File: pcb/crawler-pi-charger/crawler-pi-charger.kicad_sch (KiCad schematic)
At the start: 8 parts, among them J1 DOCK_15V, J2 SYSTEM_8V, J3 BUCK_IN_15V, J4 BUCK_OUT_8V, J5 NTC, J6 BAT_7V2, Q1 FDS6975, U1 LTC4011CFE

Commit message: Add charger MOSFETs and Wurth inductor symbols
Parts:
- added Q2: FDC658AP, Package_TO_SOT_SMD:SuperSOT-6, symbol crawler-pi-charger:FDC658AP
- added Q3: SI3434DV, Package_SO:TSOP-6_1.65x3.05mm_P0.95mm, symbol crawler-pi-charger:SI3434DV
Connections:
- net at Q1.7 (D): no longer Q1.8 (D)
- net at Q1.5 (D): no longer Q1.6 (D)
- new net SW: Q2.1 (D), Q2.2 (D), Q2.5 (D), Q2.6 (D), Q3.1 (D), Q3.2 (D), Q3.5 (D), Q3.6 (D)

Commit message: Add UPS140 Schottky diode and charger components
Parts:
- added D1: UPS140, Diode_SMD:D_Powermite_LargeCathode, symbol crawler-pi-charger:UPS140
- added L1: 10.0 uH, crawler:L_Wurth_WE-LHMI-7050, symbol crawler-pi-charger:WURTH74437349100
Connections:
- net GND: now also D1.2 (A)
- net SW: now also D1.1 (K), L1.1
- net BGATE: now reaches U1.15 (BGATE)
- net BGATE: now also Q3.3 (G)
- net TGATE: now reaches U1.17 (TGATE)
- net TGATE: now also Q2.3 (G)

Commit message: Input and PowerPath & Battery Charger (Switching Buck Converter)
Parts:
- removed J3: BUCK_IN_15V, TerminalBlock:TerminalBlock_bornier-2_P5.08mm, symbol Connector_Generic:Conn_01x02
- removed J4: BUCK_OUT_8V, TerminalBlock:TerminalBlock_bornier-2_P5.08mm, symbol Connector_Generic:Conn_01x02
- added C1, C2: 10uF, Capacitor_SMD:C_1210_3225Metric, symbol crawler-pi-charger:TMK325BJ106MM
- added D1: MMSZ5248BS-7, Diode_SMD:D_SOD-323, symbol crawler-pi-charger:MMSZ5248BS
- added R1: 47k, Resistor_SMD:R_0402_1005Metric, symbol crawler-pi-charger:CRCW040247K0JNED
- added R6: 0.05, Resistor_SMD:R_1206_3216Metric, symbol crawler-pi-charger:ERJ-L08KJ50MV
- J1: value DOCK_15V -> DOCK_12V3
- renumbered D1 to D6
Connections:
- net DOCK_15V_RAW is gone; now on net DOCK_12V3: J1.1 (Pin_1)
- net GND: now also J2.1 (Pin_1), J2.2 (Pin_2), J6.2 (Pin_2), Q1.1 (S), Q1.3 (S), Q2.4 (S), Q3.4 (S), U1.16 (PGND), U1.18 (V_{CC}), U1.21 (GND), U1.5 (GND), C1.1, C1.2, C2.2, D1.1 (K)
- net DOCK_12V3: now reaches U1.1 (DCIN)
- net DOCK_12V3: now also Q1.7 (D), Q1.8 (D), R1.1
- net SENSE: now reaches U1.11 (SENSE)
- net SENSE: now also L1.2, R6.1
- net BAT_7V2: now reaches U1.12 (BAT)
- net BAT_7V2: now also J6.1 (Pin_1), Q1.5 (D), Q1.6 (D), C2.1, R6.2
- net INFET: now reaches U1.20 (INFET)
- net INFET: now also Q1.2 (G)
- net Q1B_GATE: now reaches Q1.4 (G)
- net Q1B_GATE: now also D1.2 (A), R1.2
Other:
- moved on the sheet: D6, J2, J6, L1, Q1A, Q1B, Q2, Q3, U1

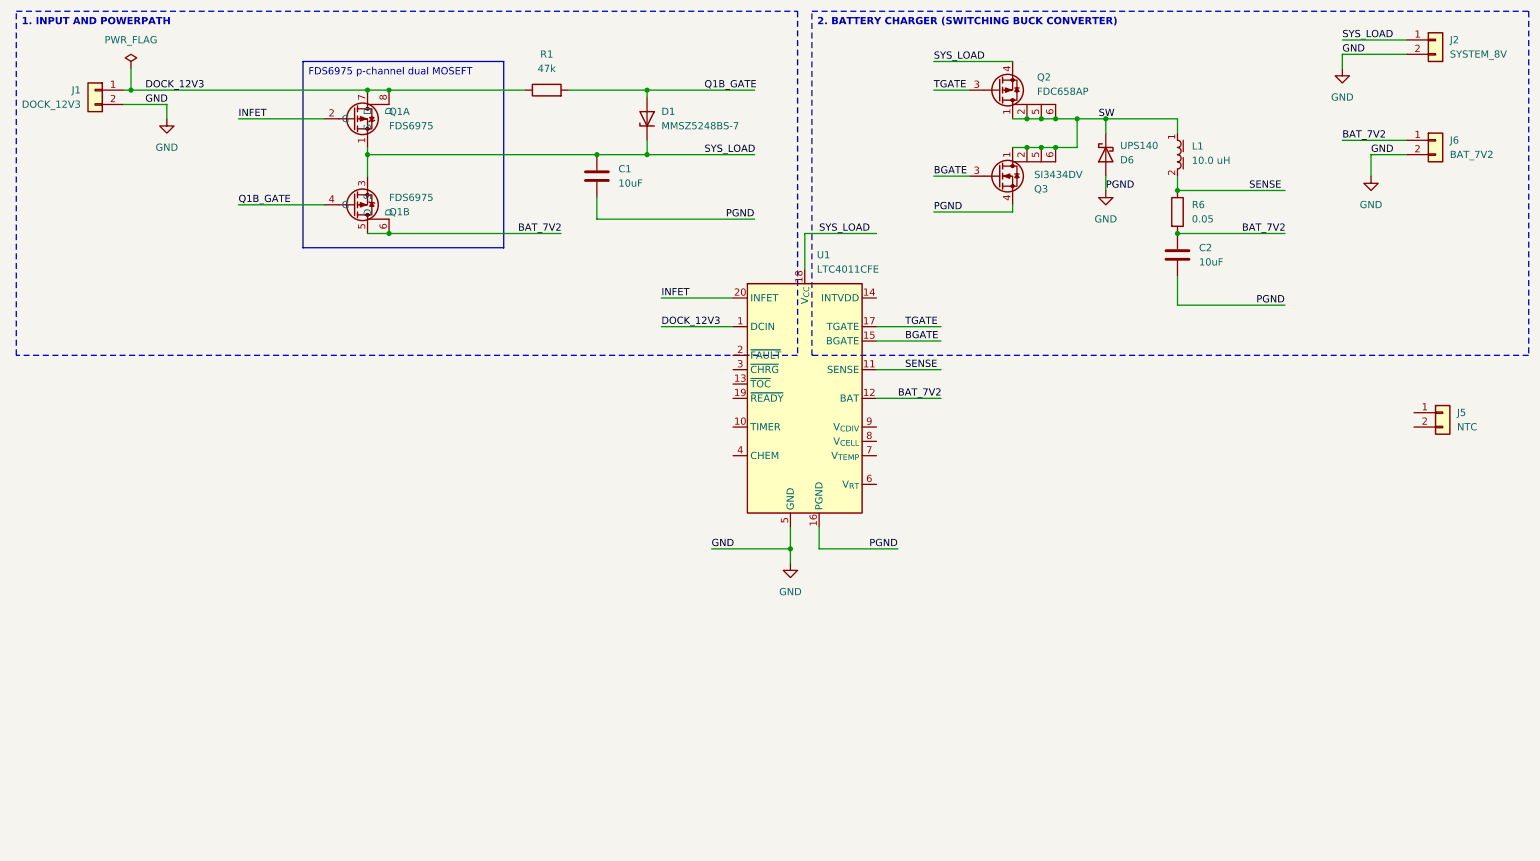
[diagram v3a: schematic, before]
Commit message: Battery Monitoring
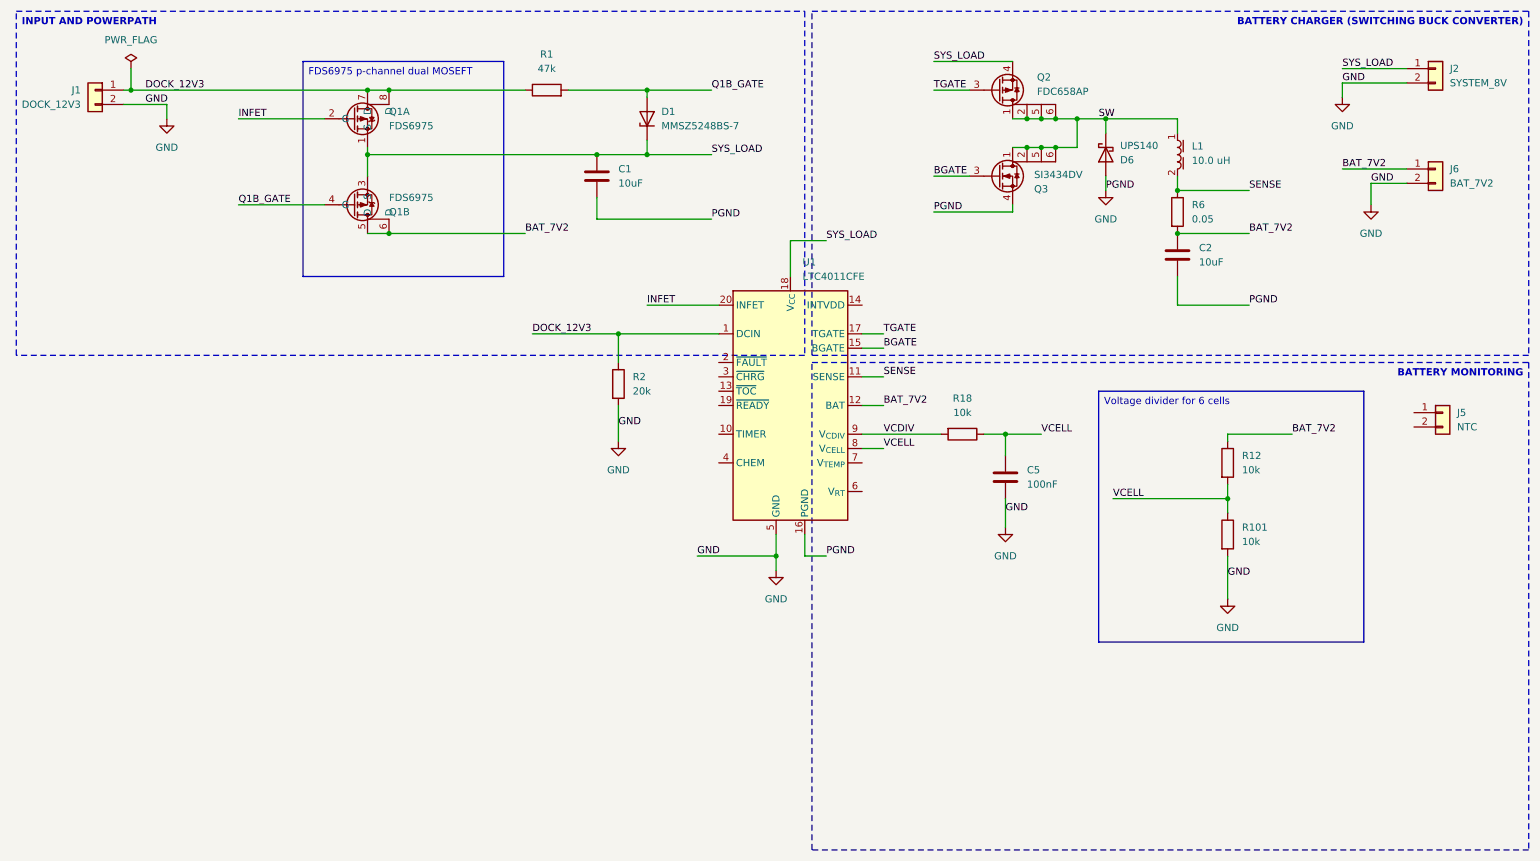
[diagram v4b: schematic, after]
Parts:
- added C5: 100nF, Capacitor_SMD:C_1210_3225Metric, symbol crawler-pi-charger:06033D104KAT2A
- added R101: 10k, Resistor_SMD:R_0603_1608Metric, symbol crawler-pi-charger:RC0603FR-0710KL
- added R12: 10k, Resistor_SMD:R_0402_1005Metric, symbol crawler-pi-charger:CRCW040249K9FKED
- added R18: 10k, Resistor_SMD:R_0402_1005Metric, symbol crawler-pi-charger:CRCW040210K0FKED
- added R2: 20k, Resistor_SMD:R_0402_1005Metric, symbol crawler-pi-charger:CRCW040220K0JNED
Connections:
- net BAT_7V2: now also R12.1
- net DOCK_12V3: now also R2.1
- net GND: now also C5.2, R101.2, R2.2
- net VCELL: now reaches U1.8 (V_{CELL})
- net VCELL: now also C5.1, R101.1, R12.2, R18.1
- net VCDIV: now reaches U1.9 (V_{CDIV})
- net VCDIV: now also R18.2
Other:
- moved on the sheet: J2, J6, U1

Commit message: Battery Voltage and Temperature Monitoring
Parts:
- removed R101: 10k, Resistor_SMD:R_0603_1608Metric, symbol crawler-pi-charger:RC0603FR-0710KL
- added C3, C4: 100nF, Capacitor_SMD:C_1210_3225Metric, symbol crawler-pi-charger:06033D104KAT2A
- added R19: 28.0K, Resistor_SMD:R_0402_1005Metric, symbol crawler-pi-charger:CRCW040228K0FKED
- added R7: 9.76k, Resistor_SMD:R_0402_1005Metric, symbol crawler-pi-charger:CRCW04029K76FKED
- added R9: 10k, Resistor_SMD:R_0402_1005Metric, symbol crawler-pi-charger:CRCW040210K0FKED
- R12: value 10k -> 49.9k
- renumbered R2 to R8
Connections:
- net GND: now also J5.2 (Pin_2), C3.2, C4.2, R19.2
- net INTVDD: now reaches U1.14 (INTVDD)
- net INTVDD: now also C3.1
- net VRT: now reaches U1.6 (V_{RT})
- net VRT: now also R7.2
- net VTEMP: now reaches U1.7 (V_{TEMP})
- net VTEMP: now also C4.1, R9.2
- net NTC: now reaches J5.1 (Pin_1)
- net NTC: now also R19.1, R7.1, R9.1
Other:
- moved on the sheet: C5, J5, R12, R18
